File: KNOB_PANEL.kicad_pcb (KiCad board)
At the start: 2 copper layers, 100 x 50 mm, 6 parts

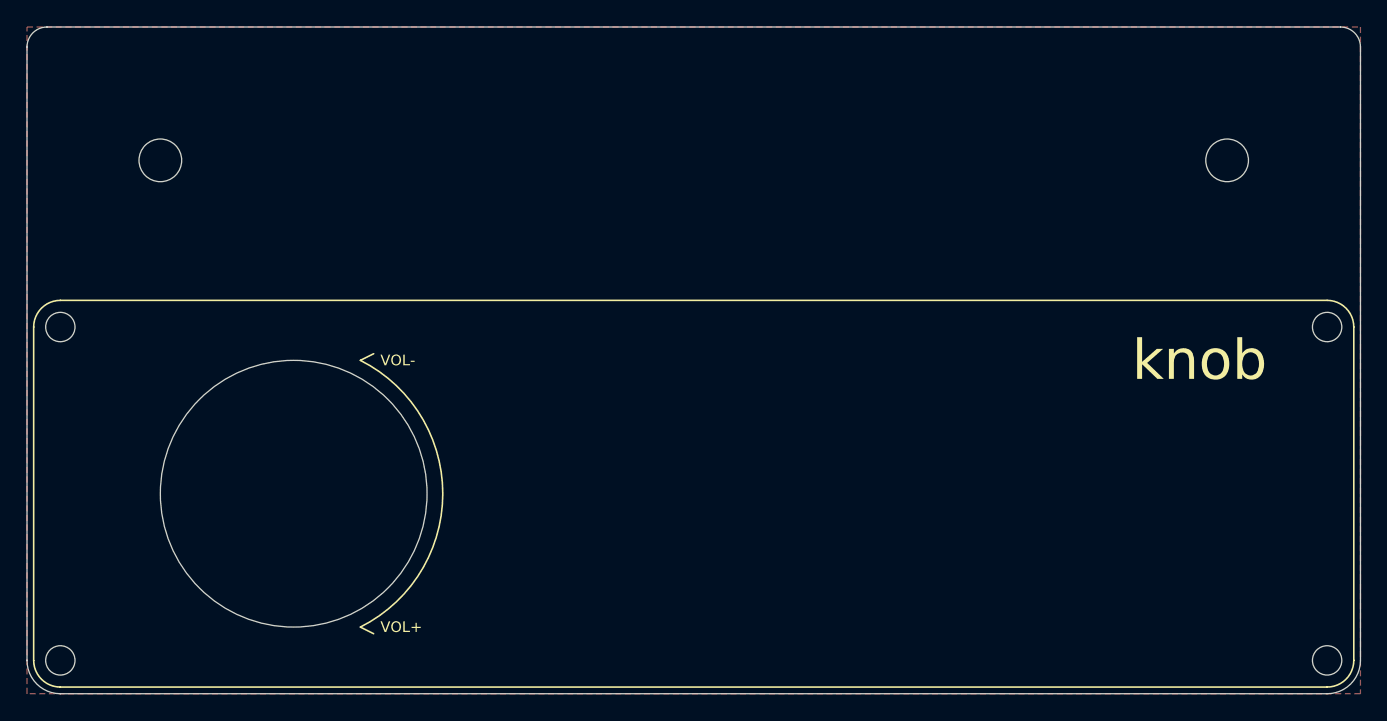
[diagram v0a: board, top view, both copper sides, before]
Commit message: Change to M3 screws
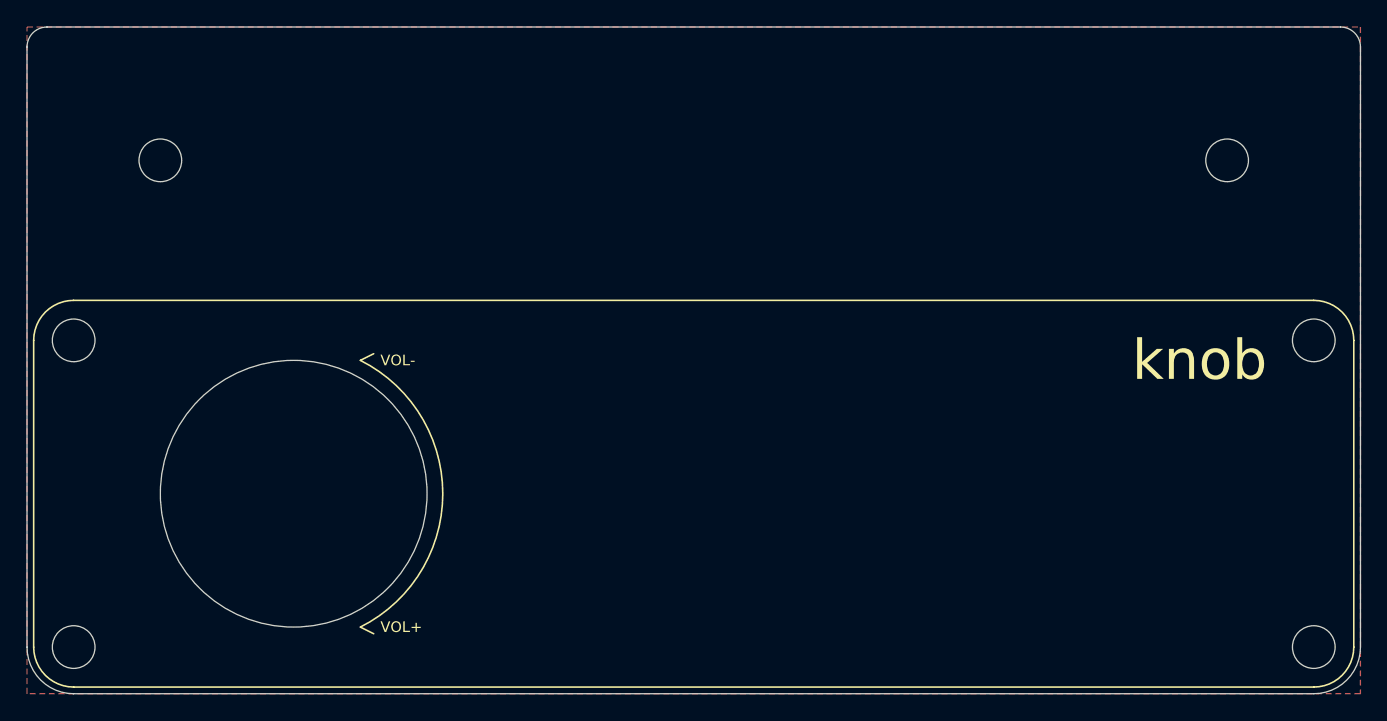
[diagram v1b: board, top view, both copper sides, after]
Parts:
- H1, H2, H3, H4: value M2 -> M3; footprint MountingHole:MountingHole_2.2mm_M2 -> MountingHole:MountingHole_3.2mm_M3
- moved H1 1.41 mm to (103.5, 73.5)
- moved H2 1.41 mm to (103.5, 96.5)
- moved H3 1.41 mm to (196.5, 73.5)
- moved H4 1.41 mm to (196.5, 96.5)
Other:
- outline, holes or cut-outs redrawn

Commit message: Output gerber
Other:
- board text added: "KNOB_PANEL V1.0 by XiNGRZ"
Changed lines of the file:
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@@
   (general
     (thickness 1.6)
-    (drawings 31)
+    (drawings 32)
     (tracks 0)
     (zones 0)
@@
       (effects (font (size 1 1) (thickness 0.15)))
     )
-    (fp_text user %R (at 0.3 0) (layer F.Fab)
-      (effects (font (size 1 1) (thickness 0.15)))
-    )
-    (fp_circle (center 0 0) (end 3.2 0) (layer Cmts.User) (width 0.15))
-    (fp_circle (center 0 0) (end 3.45 0) (layer F.CrtYd) (width 0.05))
+    (fp_circle (center 0 0) (end 3.45 0) (layer F.CrtYd) (width 0.05))
+    (fp_circle (center 0 0) (end 3.2 0) (layer Cmts.User) (width 0.15))
+    (fp_text user %R (at 0.3 0) (layer F.Fab)
+      (effects (font (size 1 1) (thickness 0.15)))
+    )
     (pad 1 np_thru_hole circle (at 0 0) (size 3.2 3.2) (drill 3.2) (layers *.Cu *.Mask))
   )
@@
       (effects (font (size 1 1) (thickness 0.15)))
     )
-    (fp_text user %R (at 0.3 0) (layer F.Fab)
-      (effects (font (size 1 1) (thickness 0.15)))
-    )
-    (fp_circle (center 0 0) (end 3.2 0) (layer Cmts.User) (width 0.15))
-    (fp_circle (center 0 0) (end 3.45 0) (layer F.CrtYd) (width 0.05))
+    (fp_circle (center 0 0) (end 3.45 0) (layer F.CrtYd) (width 0.05))
+    (fp_circle (center 0 0) (end 3.2 0) (layer Cmts.User) (width 0.15))
+    (fp_text user %R (at 0.3 0) (layer F.Fab)
+      (effects (font (size 1 1) (thickness 0.15)))
+    )
     (pad 1 np_thru_hole circle (at 0 0) (size 3.2 3.2) (drill 3.2) (layers *.Cu *.Mask))
   )
@@
       (effects (font (size 1 1) (thickness 0.15)))
     )
-    (fp_text user %R (at 0.3 0) (layer F.Fab)
-      (effects (font (size 1 1) (thickness 0.15)))
-    )
-    (fp_circle (center 0 0) (end 3.2 0) (layer Cmts.User) (width 0.15))
-    (fp_circle (center 0 0) (end 3.45 0) (layer F.CrtYd) (width 0.05))
+    (fp_circle (center 0 0) (end 3.45 0) (layer F.CrtYd) (width 0.05))
+    (fp_circle (center 0 0) (end 3.2 0) (layer Cmts.User) (width 0.15))
+    (fp_text user %R (at 0.3 0) (layer F.Fab)
+      (effects (font (size 1 1) (thickness 0.15)))
+    )
     (pad 1 np_thru_hole circle (at 0 0) (size 3.2 3.2) (drill 3.2) (layers *.Cu *.Mask))
   )
@@
       (effects (font (size 1 1) (thickness 0.15)))
     )
-    (fp_text user %R (at 0.3 0) (layer F.Fab)
-      (effects (font (size 1 1) (thickness 0.15)))
-    )
-    (fp_circle (center 0 0) (end 3.2 0) (layer Cmts.User) (width 0.15))
-    (fp_circle (center 0 0) (end 3.45 0) (layer F.CrtYd) (width 0.05))
+    (fp_circle (center 0 0) (end 3.45 0) (layer F.CrtYd) (width 0.05))
+    (fp_circle (center 0 0) (end 3.2 0) (layer Cmts.User) (width 0.15))
+    (fp_text user %R (at 0.3 0) (layer F.Fab)
+      (effects (font (size 1 1) (thickness 0.15)))
+    )
     (pad 1 np_thru_hole circle (at 0 0) (size 3.2 3.2) (drill 3.2) (layers *.Cu *.Mask))
   )
@@
       (effects (font (size 1 1) (thickness 0.15)))
     )
-    (fp_circle (center 0 0) (end 3.2 0) (layer Cmts.User) (width 0.15))
-    (fp_circle (center 0 0) (end 3.45 0) (layer F.CrtYd) (width 0.05))
+    (fp_circle (center 0 0) (end 3.45 0) (layer F.CrtYd) (width 0.05))
+    (fp_circle (center 0 0) (end 3.2 0) (layer Cmts.User) (width 0.15))
     (fp_text user %R (at 0.3 0) (layer F.Fab)
       (effects (font (size 1 1) (thickness 0.15)))
@@
       (effects (font (size 1 1) (thickness 0.15)))
     )
-    (fp_circle (center 0 0) (end 3.2 0) (layer Cmts.User) (width 0.15))
-    (fp_circle (center 0 0) (end 3.45 0) (layer F.CrtYd) (width 0.05))
-    (fp_text user %R (at 0.3 0) (layer F.Fab)
-      (effects (font (size 1 1) (thickness 0.15)))
-    )
-    (pad 1 np_thru_hole circle (at 0 0) (size 3.2 3.2) (drill 3.2) (layers *.Cu *.Mask))
+    (fp_circle (center 0 0) (end 3.45 0) (layer F.CrtYd) (width 0.05))
+    (fp_circle (center 0 0) (end 3.2 0) (layer Cmts.User) (width 0.15))
+    (fp_text user %R (at 0.3 0) (layer F.Fab)
+      (effects (font (size 1 1) (thickness 0.15)))
+    )
+    (pad 1 np_thru_hole circle (at 0 0) (size 3.2 3.2) (drill 3.2) (layers *.Cu *.Mask))
+  )
+  (gr_text "KNOB_PANEL V1.0 by XiNGRZ" (at 192 98) (layer B.SilkS)
+    (effects (font (size 1 1) (thickness 0.15)) (justify left mirror))
   )
   (gr_text knob (at 193 75) (layer F.SilkS)
